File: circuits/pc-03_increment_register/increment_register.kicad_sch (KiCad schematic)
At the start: 16 parts, among them J1 Conn_01x10, U1 74HC273, U2 74HC273, U3 74HC244, U4 74HC244

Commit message: Kicad upgrade to 9.0
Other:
- title: PC-01 Dual Register Unit -> PC-03 Increment Unit

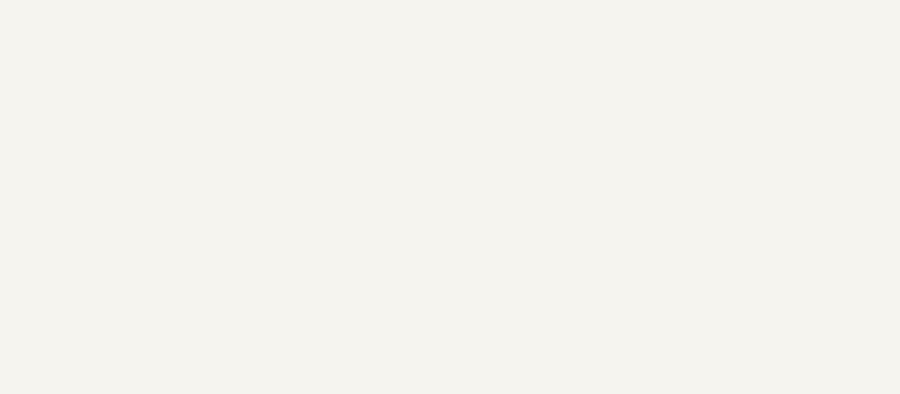
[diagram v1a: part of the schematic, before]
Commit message: add filter and decoupling capacitors to all boards
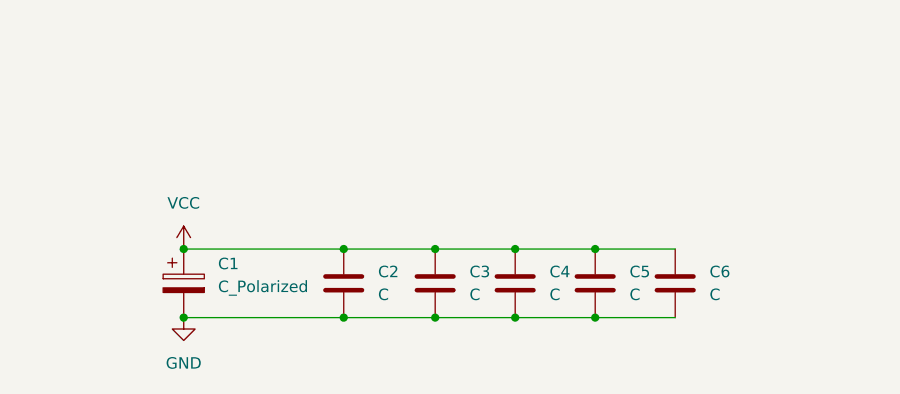
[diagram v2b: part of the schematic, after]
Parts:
- added C1: C_Polarized, Capacitor_SMD:CP_Elec_5x5.3, symbol Device:C_Polarized
- added C2, C3, C4, C5, C6: C, Capacitor_SMD:C_0603_1608Metric, symbol Device:C
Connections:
- net GND: now also C1.2, C2.2, C3.2, C4.2, C5.2, C6.2
- net VCC: now also C1.1, C2.1, C3.1, C4.1, C5.1, C6.1

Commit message: pc-03: add double buffering to incrementer unit
This ensures stable data from the incrementer.
Previously, the published address would change at the start of the write cycle.
With the double buffering introduced, the current value of the address bus is latched into the first register at the start of the write cycle and pushed to the second register at the end of the write cycle.
This way the latched address is only seen by the incrementer at the start of the next cycle, ensuring a stable address bus state during the entire program step.
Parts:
- added J3: Screw_Terminal_01x02, TerminalBlock_TE-Connectivity:TerminalBlock_TE_282834-2_1x02_P2.54mm_Horizontal, symbol Connector:Screw_Terminal_01x02
- added U14, U15: 74HC273, Package_DIP:DIP-20_W7.62mm_LongPads, symbol 74xx:74HC273
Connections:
- net GND: now also J3.1 (Pin_1), U14.10 (GND), U15.10 (GND)
- net VCC: now also J3.2 (Pin_2), U14.1 (~{Mr}), U14.20 (VCC), U15.1 (~{Mr}), U15.20 (VCC)
- net reg0: now also U14.2 (Q0); no longer U1.2 (Q0)
- net reg1: now also U14.19 (Q7); no longer U1.19 (Q7)
- net reg10: now also U15.5 (Q1); no longer U2.5 (Q1)
- net reg11: now also U15.16 (Q6); no longer U2.16 (Q6)
- net reg12: now also U15.6 (Q2); no longer U2.6 (Q2)
- net reg13: now also U15.15 (Q5); no longer U2.15 (Q5)
- net reg14: now also U15.9 (Q3); no longer U2.9 (Q3)
- net reg15: now also U15.12 (Q4); no longer U2.12 (Q4)
- net reg2: now also U14.5 (Q1); no longer U1.5 (Q1)
- net reg3: now also U14.16 (Q6); no longer U1.16 (Q6)
- net reg4: now also U14.6 (Q2); no longer U1.6 (Q2)
- net reg5: now also U14.15 (Q5); no longer U1.15 (Q5)
- net reg6: now also U14.9 (Q3); no longer U1.9 (Q3)
- net reg7: now also U14.12 (Q4); no longer U1.12 (Q4)
- net reg8: now also U15.2 (Q0); no longer U2.2 (Q0)
- net reg9: now also U15.19 (Q7); no longer U2.19 (Q7)
- new net buf0: U1.2 (Q0), U14.3 (D0)
- new net buf1: U1.19 (Q7), U14.18 (D7)
- new net buf10: U15.4 (D1), U2.5 (Q1)
- new net buf11: U15.17 (D6), U2.16 (Q6)
- new net buf12: U15.7 (D2), U2.6 (Q2)
- new net buf13: U15.14 (D5), U2.15 (Q5)
- new net buf14: U15.8 (D3), U2.9 (Q3)
- new net buf15: U15.13 (D4), U2.12 (Q4)
- new net buf2: U1.5 (Q1), U14.4 (D1)
- new net buf3: U1.16 (Q6), U14.17 (D6)
- new net buf4: U1.6 (Q2), U14.7 (D2)
- new net buf5: U1.15 (Q5), U14.14 (D5)
- new net buf6: U1.9 (Q3), U14.8 (D3)
- new net buf7: U1.12 (Q4), U14.13 (D4)
- new net buf8: U15.3 (D0), U2.2 (Q0)
- new net buf9: U15.18 (D7), U2.19 (Q7)
- new net ~{clock}: U14.11 (Cp), U15.11 (Cp)
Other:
- moved on the sheet: ADDRESS_BUS1, C1, C2, C3, C4, C5, C6, DATA_BUS1, R1, R2, R3, R4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
